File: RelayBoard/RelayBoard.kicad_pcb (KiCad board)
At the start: 2 copper layers, 88.6 x 38.1 mm, 59 parts, among them J1 Micro_SD_Card, J10 Conn_01x04_Male, J11 Conn_01x04_Male, J13 Conn_01x04_Male, J2 Screw_Terminal_01x02, J3 Conn_01x04_Male, J4 Conn_01x04_Male, J5 Conn_01x04_Male, J7 SI-52008-F, J8 SI-52008-F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

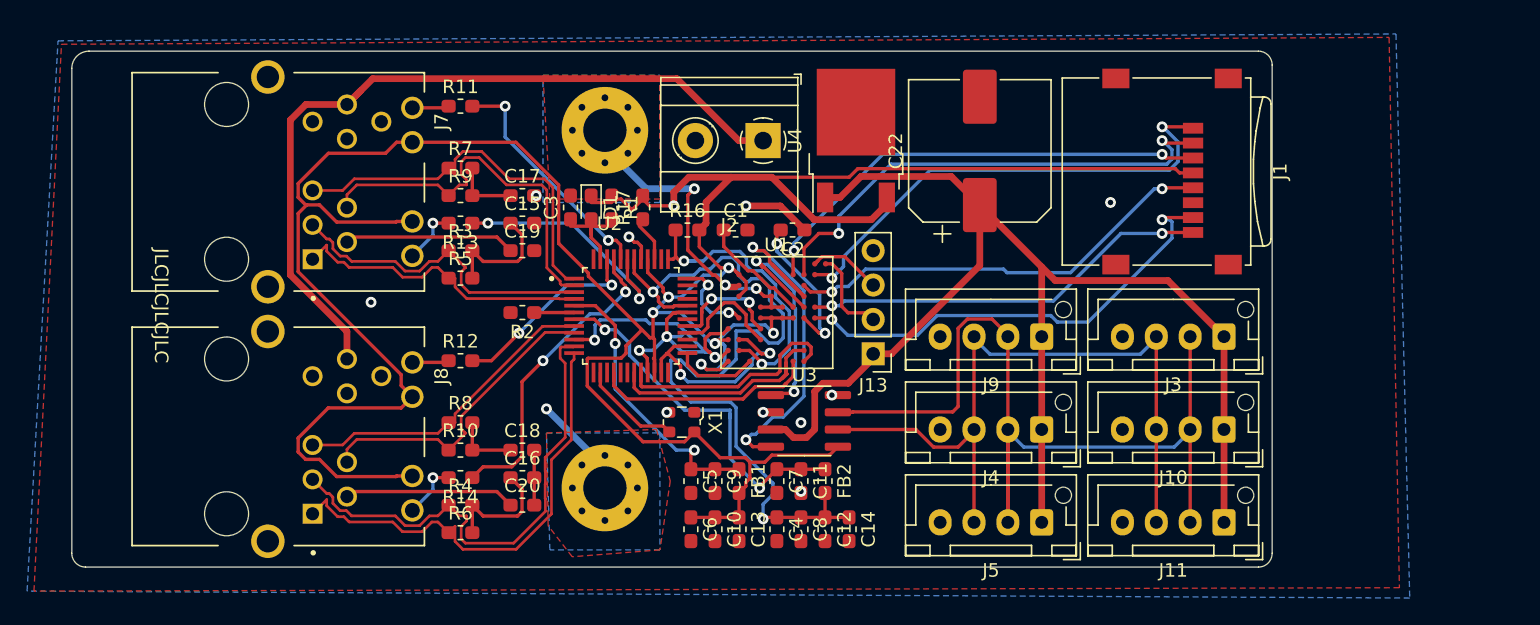
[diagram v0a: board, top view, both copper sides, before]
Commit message: unnecessary but satisfying miniaturization
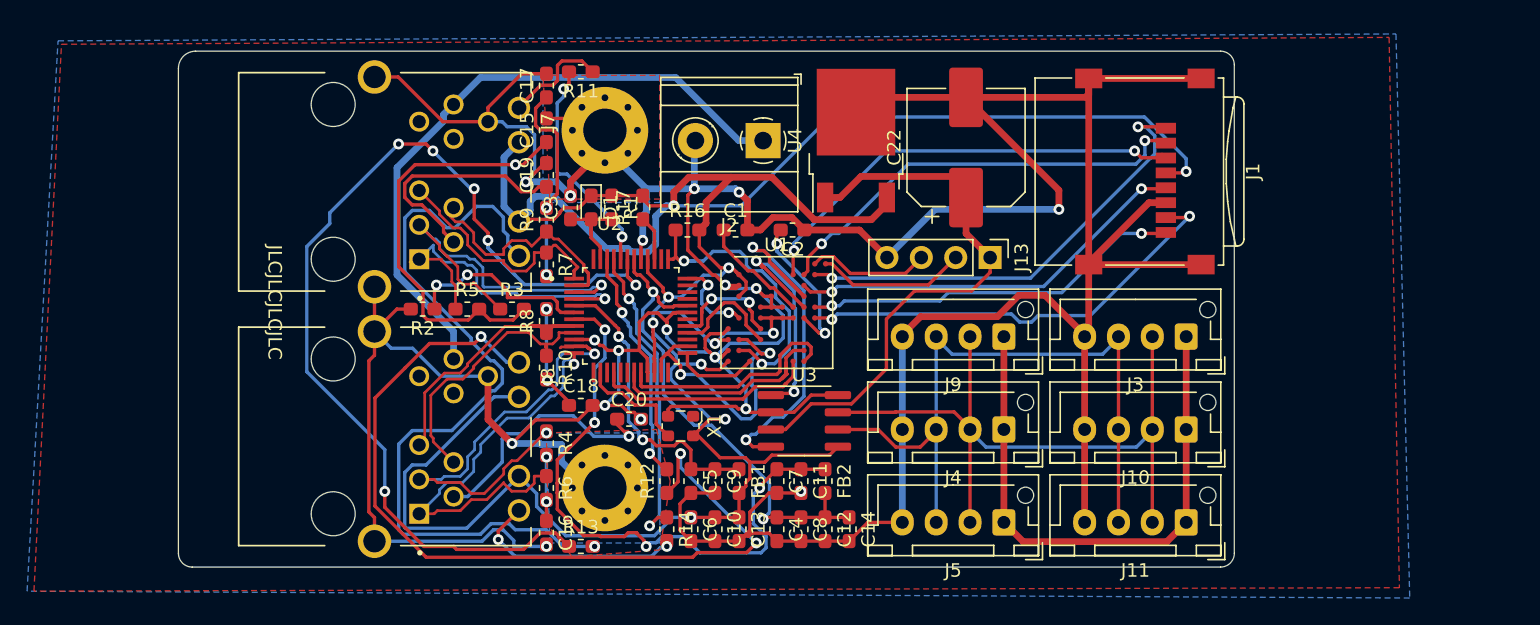
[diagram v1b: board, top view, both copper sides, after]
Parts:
- C22: value 330uF EMZS350ARA331MHA0G -> 1000uF EEE-FT1A102AV; footprint Capacitor_SMD:CP_Elec_10x10 -> Capacitor_SMD:CP_Elec_8x10.5
- moved R13 25.5 mm to (128.8, 98.0), turned to 0 degrees
- moved R12 17.6 mm to (135.1, 93.2), turned to 90 degrees
- moved R14 15.7 mm to (135.1, 96.8), turned to 270 degrees
- moved J13 11.2 mm to (159.0, 76.7), turned to 270 degrees
- moved C20 10.1 mm to (132.3, 88.6)
- moved R8 9.83 mm to (126.2, 81.4), turned to 90 degrees
- moved R7 9.53 mm to (126.2, 77.2), turned to 270 degrees
- moved R11 9.25 mm to (128.8, 63.0), turned to 180 degrees
- moved R10 8.80 mm to (126.2, 84.8), turned to 270 degrees
- moved G*** 8.42 mm to (102.6, 80.8)
- moved C17 8.32 mm to (126.2, 64.0), turned to 90 degrees
- moved J7 7.87 mm to (110.5, 71.1)
- moved J8 7.87 mm to (110.5, 89.9)
- moved R4 7.82 mm to (126.2, 90.4), turned to 270 degrees
- moved R2 7.37 mm to (117.1, 80.5)
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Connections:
- J10 pad 1: 5V -> 5V_CAN
- J11 pad 1: 5V -> 5V_CAN
- J3 pad 1: 5V -> 5V_CAN
- J4 pad 1: 5V -> 5V_CAN
- J5 pad 1: 5V -> 5V_CAN
- J7 pad 8: Net-(J7-Pad8) -> (no net)
- J7 pad 9: Net-(J7-Pad9) -> (no net)
- J8 pad 8: Net-(J8-Pad8) -> (no net)
- J8 pad 9: Net-(J8-Pad9) -> (no net)
- J9 pad 1: 5V -> 5V_CAN
- U2 pad 15: Net-(U2-Pad15) -> (no net)
- U2 pad 17: Net-(U2-Pad17) -> (no net)
- U2 pad 18: Net-(U2-Pad18) -> (no net)
- U2 pad 24: Net-(U2-Pad24) -> (no net)
- U2 pad 27: Net-(U2-Pad27) -> (no net)
- U2 pad 30: Net-(U2-Pad30) -> (no net)
- U2 pad 33: Net-(U2-Pad33) -> (no net)
- U2 pad 34: Net-(U2-Pad34) -> (no net)
- U2 pad 35: Net-(U2-Pad35) -> (no net)
- U2 pad 38: Net-(U2-Pad38) -> (no net)
- U2 pad 48: Net-(U2-Pad48) -> (no net)
- X1 pad 1: Net-(X1-Pad1) -> (no net)
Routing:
- net GND: track 80.1 -> 416.2 mm
- net Net-(J8-PadG_K): track 2.73 -> 64.0 mm, vias 0 -> 3
- net P1LED2: track 18.3 -> 77.8 mm, vias 2 -> 6
- net Net-(J7-PadY_A): track 4.20 -> 59.1 mm
- net 5V: track 94.5 -> 42.4 mm
- net 5V_CAN: track 0.00 -> 42.1 mm
- net Net-(C15-Pad1): track 9.03 -> 31.6 mm, vias 0 -> 1
- net VDDC: track 58.6 -> 36.5 mm
- net VDDA_1.8: track 27.2 -> 45.7 mm, vias 2 -> 4
- net CANH: track 69.0 -> 53.1 mm
- net Net-(J8-PadY_A): track 4.20 -> 16.2 mm, vias 1 -> 2
- net Net-(R2-Pad1): track 2.95 -> 14.1 mm, vias 0 -> 2
- net 24V: track 59.8 -> 48.7 mm
- net RX1-: track 28.8 -> 18.3 mm
- net RX1+: track 28.5 -> 18.0 mm
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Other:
- board size 88.6 x 38.1 mm -> 78 x 38.1 mm
- rule via_min_size: 0.4 -> 0.8

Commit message: cleanup; bump to v1.2
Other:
- board text added: "Relay Board v1.2 by Clive Chan"
- board text removed: "Relay Board v1.1 by Clive Chan"

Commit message: ... and now it's even smaller.
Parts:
- removed J5, J9: Conn_01x04_Male, Connector_JST:JST_XH_B4B-XH-AM_1x04_P2.50mm_Vertical
- added J12: 505004-0812, SamacSys_Parts:5050040812, B.Cu at (110.5, 71.1)
- added R15: 300mOhm, Resistor_SMD:R_0805_2012Metric_Pad1.15x1.40mm_HandSolder, F.Cu at (163.8, 69.8)
- J10, J11, J4: value Conn_01x04_Male -> 505004-0812; footprint Connector_JST:JST_XH_B4B-XH-AM_1x04_P2.50mm_Vertical -> SamacSys_Parts:5050040812; moved to B.Cu
- moved J11 63.3 mm to (110.5, 89.9), turned to 90 degrees
- moved G*** 49.5 mm to (149.9, 66.0), turned to 180 degrees
- moved J1 23.7 mm to (158.2, 90.7)
- moved J4 23.6 mm to (159.3, 65.8), turned to 90 degrees
- moved J10 15.4 mm to (159.3, 95.2), turned to 90 degrees
- moved J3 14.8 mm to (159.0, 79.5)
- moved J13 6.35 mm to (164.1, 72.9), turned to 0 degrees
- moved C22 0.51 mm to (157.2, 69.1)
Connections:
- J13 pad 1: 5V -> 5V_CAN
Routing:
- net 3V3: track 222.3 -> 190.1 mm, vias 10 -> 9
- net GND: track 416.2 -> 394.8 mm, vias 18 -> 19
- net 5V_CAN: track 42.1 -> 21.1 mm, vias 0 -> 1
- net SD_D2: track 34.0 -> 17.9 mm
- net SWDIO: track 11.1 -> 24.3 mm
- net CANL: track 50.9 -> 38.6 mm
- net CANH: track 53.1 -> 41.1 mm
- net SWCLK: track 9.08 -> 19.9 mm
- net SD_D0: track 33.2 -> 24.1 mm
- net SD_CLK: track 30.2 -> 21.4 mm
- net SD_D3: track 32.4 -> 24.1 mm
- net SD_CMD: track 33.2 -> 28.1 mm
- net SD_D1: track 28.3 -> 23.8 mm
- net P1LED2: track 77.8 -> 81.6 mm
- net 5V: track 42.4 -> 45.2 mm, vias 0 -> 2
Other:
- board size 78 x 38.1 mm -> 59.2 x 38.1 mm
- net class Default: clearance 0.2 -> 0.15
- rule trace_clearance: 0.2 -> 0.15

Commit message: octopus!
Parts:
- added G***: LOGO, Waterloop:octopus, B.Cu at (136.4, 81.5)
- moved G*** 2.40 mm to (148.6, 68.1)
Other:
- board text added: "Relay Board v1.3 by Clive Chan"
- board text removed: "Relay Board v1.2 by Clive Chan"

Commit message: better grounding etc
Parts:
- removed the G*** at (136.4, 81.5)
- added R18: 120Ω, Resistor_SMD:R_0603_1608Metric_Pad1.05x0.95mm_HandSolder, F.Cu at (148.6, 93.2)
- H1, H2: renamed from REF**; value MountingHole_3.2mm_M3_Pad_Via -> MountingHole_Pad
- R15: value 300mOhm -> 300mΩ
- X1: value ECS-2520MV-xxx-xx -> ECS-2520SMV-250-GP-TR
- moved R13 25.5 mm to (110.2, 80.5)
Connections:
- C1 pad 2: GND -> GNDC
- C10 pad 2: GND -> GNDC
- C11 pad 2: GND -> GNDC
- C12 pad 2: GND -> GNDC
- C13 pad 2: GND -> GNDC
- C14 pad 2: GND -> GNDC
- C15 pad 2: GND -> GNDC
- C16 pad 2: GND -> GNDC
- C17 pad 2: GND -> GNDC
- C18 pad 2: GND -> GNDC
- C19 pad 2: GND -> GNDC
- C2 pad 1: GND -> GNDC
- C20 pad 2: GND -> GNDC
- C22 pad 2: GND -> GNDC
- C3 pad 2: GND -> GNDC
- C4 pad 2: GND -> GNDC
- C5 pad 2: GND -> GNDC
- C6 pad 2: GND -> GNDC
- C7 pad 2: GND -> GNDC
- C8 pad 2: GND -> GNDC
- C9 pad 2: GND -> GNDC
- H1 pad 1: GND -> GNDC
- H2 pad 1: GND -> GNDC
- J1 pad 6: GND -> GNDC
- J1 pad 9: GND -> GNDC
- J10 pad P1: GND -> GNDC
- J10 pad P2: GND -> GNDC
- J10 pad P3: GND -> GNDC
- J10 pad P4: GND -> GNDC
- J11 pad P1: GND -> GNDC
- J11 pad P2: GND -> GNDC
- J11 pad P3: GND -> GNDC
- J11 pad P4: GND -> GNDC
- J12 pad P1: GND -> GNDC
- J12 pad P2: GND -> GNDC
- J12 pad P3: GND -> GNDC
- J12 pad P4: GND -> GNDC
- J13 pad 4: GND -> GNDC
- J2 pad 2: GND -> GND24
- J3 pad 4: GND -> GNDC
- J4 pad MP1: GND -> (no net)
- J4 pad MP2: GND -> (no net)
- J4 pad MP3: GND -> (no net)
- J4 pad MP4: GND -> (no net)
- J4 pad P3: GND -> GNDC
- J4 pad P4: GND -> GNDC
- J7 pad 11: GND -> GND24
- J7 pad S1: GND -> GNDC
- J7 pad S2: GND -> GNDC
- J8 pad 11: GND -> GND24
- J8 pad S1: GND -> GNDC
- J8 pad S2: GND -> GNDC
- R2 pad 2: GND -> GNDC
- U1 pad C2: GND -> GNDC
- U1 pad D5: GND -> GNDC
- U1 pad E4: GND -> GNDC
- U1 pad E5: GND -> GNDC
- U1 pad E6: GND -> GNDC
- U1 pad G1: GND -> GNDC
- U1 pad J1: GND -> GNDC
- U2 pad 10: GND -> GNDC
- U2 pad 21: GND -> GNDC
- U2 pad 31: GND -> GNDC
- U2 pad 41: GND -> GNDC
- U3 pad 2: GND -> GNDC
- U3 pad 8: GND -> GNDC
- U4 pad 2: GND -> GNDC
- X1 pad 2: GND -> GNDC
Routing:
- net GND: track 394.8 -> 0.00 mm, vias 19 -> 0
- net GNDC: track 0.00 -> 376.8 mm, vias 0 -> 40
- net GND24: track 0.00 -> 47.5 mm
- net P1LED2: track 81.6 -> 36.6 mm, vias 6 -> 2
- net Net-(J7-PadY_A): track 59.1 -> 18.8 mm
- net 24V: track 48.7 -> 60.6 mm
- net CANH: track 41.1 -> 49.4 mm, vias 0 -> 2
- net CANL: track 38.6 -> 43.5 mm, vias 0 -> 2
- net VDDC: track 36.5 -> 37.1 mm
- net 3V3: track 190.1 -> 190.6 mm
- added copper zone on B.Cu, net GNDC
- added copper zone on F.Cu, net GNDC
- removed copper zone on B.Cu, net GND
- removed copper zone on F.Cu, net GND

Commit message: final edits during sourcing; submitted for printing
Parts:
- added G***: LOGO, Waterloop:octopus, B.Cu at (133.6, 80.3)
- G***: moved to F.Cu
- J1: footprint Connector_Card:microSD_HC_Wuerth_693072010801 -> SamacSys_Parts:PJS008U30000
- J2: footprint TerminalBlock_Phoenix:TerminalBlock_Phoenix_MKDS-1,5-2_1x02_P5.00mm_Horizontal -> SamacSys_Parts:1725656
- J3: footprint Connector_JST:JST_XH_B4B-XH-AM_1x04_P2.50mm_Vertical -> Connector_JST:JST_XH_B4B-XH-A_1x04_P2.50mm_Vertical
- moved R15 32.3 mm to (132.3, 62.7)
- moved J13 20.6 mm to (145.3, 64.5)
- moved C22 18.6 mm to (138.7, 67.8)
- moved J3 16.9 mm to (151.1, 64.5), turned to 270 degrees
- moved J2 14.8 mm to (157.0, 68.8)
- moved U4 11.8 mm to (154.2, 78.7), turned to 180 degrees
- moved G*** 9.01 mm to (157.0, 64.8), turned to 90 degrees
- moved J1 5.97 mm to (152.3, 90.2)
- moved J10 2.29 mm to (157.0, 95.2)
- moved J4 2.29 mm to (157.0, 65.8)
- moved C12 1.02 mm to (145.8, 96.8)
- moved FB2 1.02 mm to (145.8, 93.2)
- moved C11 1.02 mm to (144.0, 93.2)
- moved C14 1.02 mm to (147.6, 96.8)
- moved C4 1.02 mm to (142.2, 96.8)
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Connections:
- J2 pad 1: 24V -> GND24
- J2 pad 2: GND24 -> 24V
- J4 pad S1: CANH -> CANL
- J4 pad S2: CANL -> CANH
- J4 pad S3: CANL -> CANH
- J4 pad S4: CANH -> CANL
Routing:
- net GND24: track 47.5 -> 72.1 mm
- net 24V: track 60.6 -> 80.6 mm
- net 5V: track 45.2 -> 58.8 mm, vias 2 -> 3
- net SWDIO: track 24.3 -> 13.6 mm
- net 5V_CAN: track 21.1 -> 31.0 mm, vias 1 -> 0
- net SWCLK: track 19.9 -> 10.2 mm
- net 3V3: track 190.6 -> 182.0 mm, vias 9 -> 10
- net SD_D0: track 24.1 -> 15.7 mm, vias 2 -> 1
- net VDDA_1.8: track 45.7 -> 52.1 mm
- net SD_D3: track 24.1 -> 18.0 mm, vias 2 -> 1
- net SD_D2: track 17.9 -> 12.2 mm, vias 2 -> 1
- net SD_CMD: track 28.1 -> 22.4 mm, vias 2 -> 1
- net SD_CLK: track 21.4 -> 16.7 mm, vias 2 -> 1
- net GNDC: track 376.8 -> 380.5 mm, vias 40 -> 24
- net SD_D1: track 23.8 -> 20.3 mm, vias 2 -> 1
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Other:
- board size 59.2 x 38.1 mm -> 52.8 x 38.1 mm
- board text added: "Relay Board v1.4 by Clive Chan"
- board text removed: "Relay Board v1.3 by Clive Chan"
